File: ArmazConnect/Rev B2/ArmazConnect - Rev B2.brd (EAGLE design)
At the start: 165 x 74 mm, 43 parts, among them X0 NC3FAAV2, X1 NC3FAAV2, X2 NC3FAAV2, X3 NC3FAAV2, X4 NC5FAV-SW, X5 NC5MAV-SW, X6 NC5FAV-SW, X8 87832-26

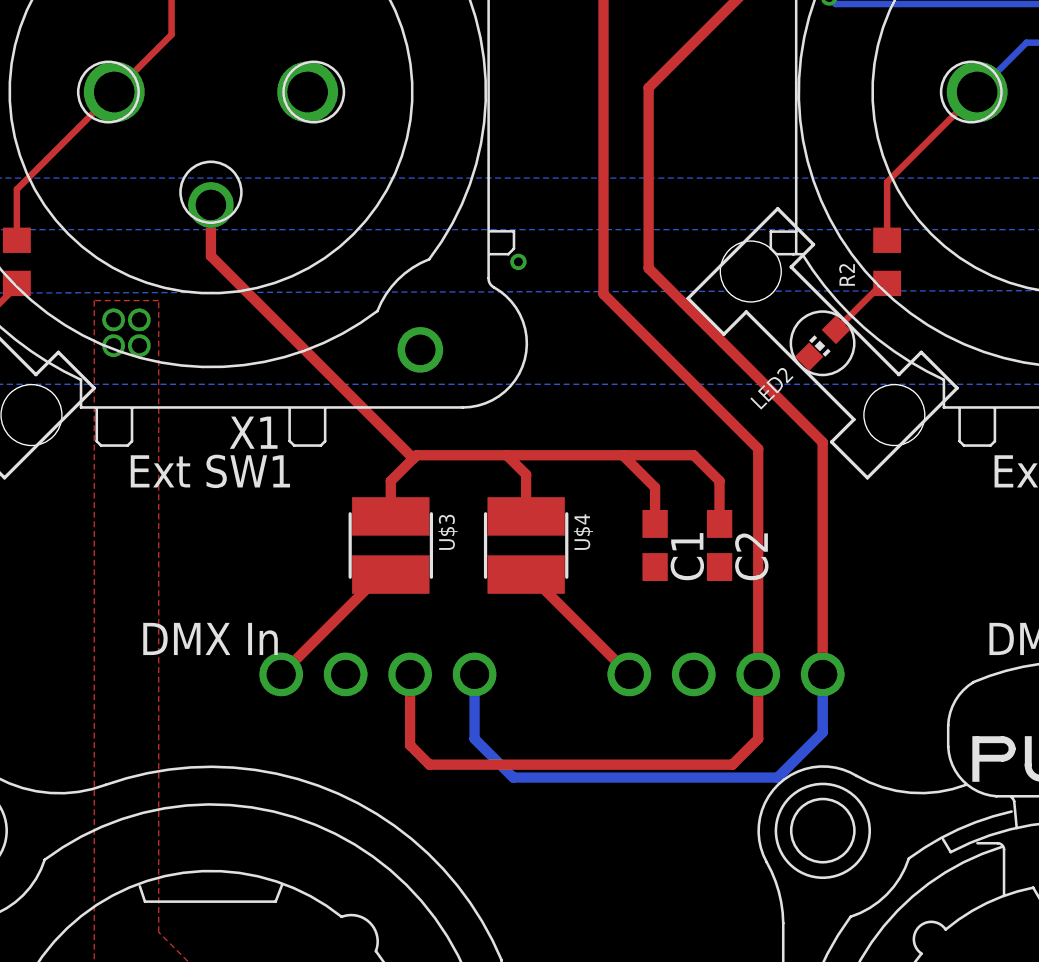
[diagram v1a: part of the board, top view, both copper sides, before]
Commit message: Update routing of ArmazConnect- Rev B2 (creation of polygon for +5V and GND1)
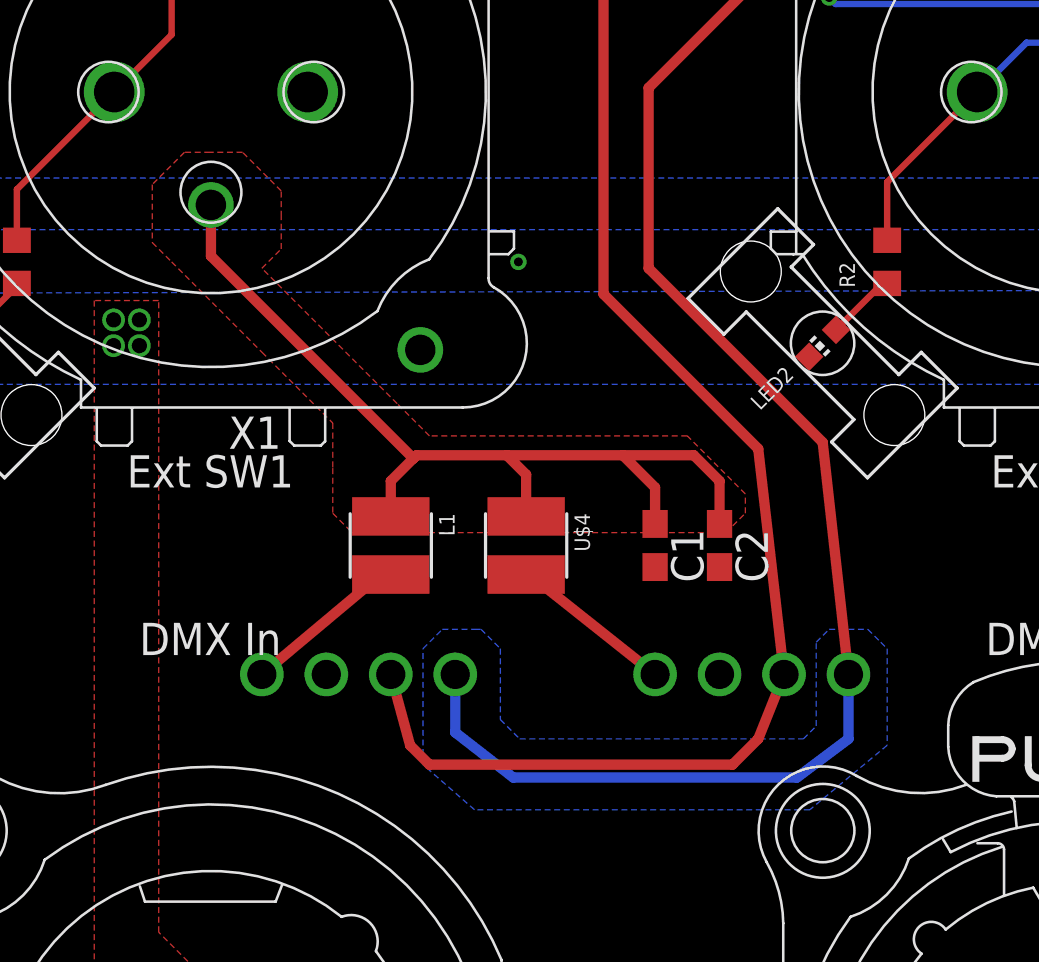
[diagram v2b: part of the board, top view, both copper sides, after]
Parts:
- removed U$1, U$2: MEE3S1205SC, dc-dc-converter:MEE3
- added DC1, DC2: MEE3S1205SC, dc-dc-converter:MEE3
- renumbered U$3 to L1
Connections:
- net +12V: now also DC1.2, DC2.2; no longer U$1.2, U$2.2
- net GND: now also DC1.3, DC2.3; no longer U$1.3, U$2.3
- net GND1: now also DC1.1, DC2.1; no longer U$1.1, U$2.1
- net N$5: now also DC1.4; no longer U$1.4
- net N$7: now also DC2.4; no longer U$2.4
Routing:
- net GND1: track 132.7 -> 134.3 mm
- net N$7: track 5.69 -> 6.45 mm
- net N$5: track 5.95 -> 6.51 mm
- added copper zone on layer 16, net GND1
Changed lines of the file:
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@@
 <grid distance="10" unitdist="mil" unit="mil" style="lines" multiple="1" display="no" altdistance="0.5" altunitdist="mm" altunit="mm"/>
 <layers>
-<layer number="1" name="Top" color="4" fill="1" visible="yes" active="yes"/>
+<layer number="1" name="Top" color="4" fill="1" visible="no" active="yes"/>
 <layer number="2" name="Route2" color="1" fill="3" visible="no" active="no"/>
 <layer number="3" name="Route3" color="4" fill="3" visible="no" active="no"/>
@@
 <layer number="19" name="Unrouted" color="6" fill="1" visible="yes" active="yes"/>
 <layer number="20" name="Dimension" color="15" fill="1" visible="yes" active="yes"/>
-<layer number="21" name="tPlace" color="7" fill="1" visible="yes" active="yes"/>
+<layer number="21" name="tPlace" color="7" fill="1" visible="no" active="yes"/>
 <layer number="22" name="bPlace" color="7" fill="1" visible="yes" active="yes"/>
-<layer number="23" name="tOrigins" color="15" fill="1" visible="yes" active="yes"/>
+<layer number="23" name="tOrigins" color="15" fill="1" visible="no" active="yes"/>
 <layer number="24" name="bOrigins" color="15" fill="1" visible="yes" active="yes"/>
-<layer number="25" name="tNames" color="7" fill="1" visible="yes" active="yes"/>
+<layer number="25" name="tNames" color="7" fill="1" visible="no" active="yes"/>
 <layer number="26" name="bNames" color="7" fill="1" visible="yes" active="yes"/>
-<layer number="27" name="tValues" color="7" fill="1" visible="yes" active="yes"/>
+<layer number="27" name="tValues" color="7" fill="1" visible="no" active="yes"/>
 <layer number="28" name="bValues" color="7" fill="1" visible="yes" active="yes"/>
 <layer number="29" name="tStop" color="7" fill="3" visible="no" active="yes"/>
@@
 <layer number="49" name="Reference" color="7" fill="1" visible="yes" active="yes"/>
 <layer number="50" name="dxf" color="7" fill="1" visible="no" active="no"/>
-<layer number="51" name="tDocu" color="7" fill="1" visible="yes" active="yes"/>
+<layer number="51" name="tDocu" color="7" fill="1" visible="no" active="yes"/>
 <layer number="52" name="bDocu" color="7" fill="1" visible="yes" active="yes"/>
 <layer number="53" name="tGND_GNDA" color="7" fill="1" visible="no" active="no"/>
@@
 <attribute name="VALUE" x="136.906" y="57.912" size="0.4064" layer="27" ratio="10"/>
 </element>
-<element name="U$1" library="dc-dc-converter" package="MEE3" value="MEE3S1205SC" x="48.768" y="35.052" rot="MR0"/>
-<element name="U$2" library="dc-dc-converter" package="MEE3" value="MEE3S1205SC" x="62.484" y="35.052" rot="MR0"/>
-<element name="U$3" library="murata-inductance" package="8200" value="10uH" x="53.086" y="40.132" rot="R180"/>
+<element name="DC1" library="dc-dc-converter" package="MEE3" value="MEE3S1205SC" x="48.006" y="35.052" rot="MR0"/>
+<element name="DC2" library="dc-dc-converter" package="MEE3" value="MEE3S1205SC" x="63.5" y="35.052" rot="MR0"/>
+<element name="L1" library="murata-inductance" package="8200" value="10uH" x="53.086" y="40.132" rot="R180"/>
 <element name="U$4" library="murata-inductance" package="8200" value="10uH" x="58.42" y="40.132" rot="R180"/>
 <element name="C1" library="rcl" package="C0603" value="4.7uF" x="63.5" y="40.132" rot="R270"/>
@@
 <contactref element="C1" pad="2"/>
 <contactref element="C2" pad="2"/>
-<contactref element="U$2" pad="3"/>
-<contactref element="U$1" pad="3"/>
+<contactref element="DC2" pad="3"/>
+<contactref element="DC1" pad="3"/>
 </signal>
 <signal name="N$27">
@@
 <wire x1="137.414" y1="59.248" x2="137.8" y2="59.248" width="0.4064" layer="1"/>
 <wire x1="137.8" y1="59.248" x2="137.822" y2="59.27" width="0.4064" layer="1"/>
-<contactref element="U$3" pad="2"/>
+<contactref element="L1" pad="2"/>
 <contactref element="U$4" pad="2"/>
 <contactref element="C2" pad="1"/>
@@
 <wire x1="46" y1="53.55" x2="46" y2="51.536" width="0.4064" layer="1"/>
 <wire x1="46" y1="51.536" x2="53.975" y2="43.561" width="0.4064" layer="1"/>
+<polygon width="0.4064" layer="1">
+<vertex x="45.974" y="55.626"/>
+<vertex x="44.958" y="55.626"/>
+<vertex x="43.688" y="54.356"/>
+<vertex x="43.688" y="52.07"/>
+<vertex x="44.45" y="51.308"/>
+<vertex x="48.006" y="47.752"/>
+<vertex x="50.8" y="44.958"/>
+<vertex x="50.8" y="43.18"/>
+<vertex x="50.8" y="41.402"/>
+<vertex x="51.562" y="40.64"/>
+<vertex x="65.786" y="40.64"/>
+<vertex x="66.294" y="40.64"/>
+<vertex x="67.056" y="41.402"/>
+<vertex x="67.056" y="42.164"/>
+<vertex x="64.77" y="44.45"/>
+<vertex x="54.61" y="44.45"/>
+<vertex x="53.34" y="45.72"/>
+<vertex x="48.006" y="51.054"/>
+<vertex x="48.768" y="51.816"/>
+<vertex x="48.768" y="53.086"/>
+<vertex x="48.768" y="54.102"/>
+<vertex x="47.244" y="55.626"/>
+</polygon>
 </signal>
 <signal name="ESW0">
@@
 <via x="72.39" y="70.104" extent="1-16" drill="0.35" shape="square"/>
 <via x="71.628" y="70.104" extent="1-16" drill="0.35" shape="square"/>
-<contactref element="U$1" pad="2"/>
-<contactref element="U$2" pad="2"/>
-<wire x1="53.848" y1="35.052" x2="53.848" y2="32.258" width="0.4064" layer="1"/>
+<contactref element="DC1" pad="2"/>
+<contactref element="DC2" pad="2"/>
+<wire x1="53.086" y1="35.052" x2="53.848" y2="32.258" width="0.4064" layer="1"/>
 <wire x1="53.848" y1="32.258" x2="54.61" y2="31.496" width="0.4064" layer="1"/>
 <wire x1="54.61" y1="31.496" x2="66.548" y2="31.496" width="0.4064" layer="1"/>
 <wire x1="66.548" y1="31.496" x2="67.564" y2="32.512" width="0.4064" layer="1"/>
-<wire x1="67.564" y1="32.512" x2="67.564" y2="35.052" width="0.4064" layer="1"/>
-<wire x1="67.564" y1="35.052" x2="67.564" y2="43.942" width="0.4064" layer="1"/>
+<wire x1="67.564" y1="32.512" x2="68.58" y2="35.052" width="0.4064" layer="1"/>
+<wire x1="68.58" y1="35.052" x2="67.564" y2="43.942" width="0.4064" layer="1"/>
 <wire x1="67.564" y1="43.942" x2="61.468" y2="50.038" width="0.4064" layer="1"/>
 <wire x1="61.468" y1="50.038" x2="61.468" y2="69.85" width="0.4064" layer="1"/>
@@
 <wire x1="68.508" y1="63.246" x2="68" y2="63.754" width="0.4064" layer="16"/>
 <via x="68" y="63.754" extent="1-16" drill="0.35"/>
-<contactref element="U$1" pad="1"/>
-<contactref element="U$2" pad="1"/>
-<wire x1="56.388" y1="35.052" x2="56.388" y2="32.512" width="0.4064" layer="16"/>
-<wire x1="56.388" y1="32.512" x2="57.912" y2="30.988" width="0.4064" layer="16"/>
-<wire x1="57.912" y1="30.988" x2="68.326" y2="30.988" width="0.4064" layer="16"/>
-<wire x1="68.326" y1="30.988" x2="70.104" y2="32.766" width="0.4064" layer="16"/>
-<wire x1="70.104" y1="32.766" x2="70.104" y2="35.052" width="0.4064" layer="16"/>
-<wire x1="70.104" y1="35.052" x2="70.104" y2="44.196" width="0.4064" layer="1"/>
+<contactref element="DC1" pad="1"/>
+<contactref element="DC2" pad="1"/>
+<wire x1="55.626" y1="35.052" x2="55.626" y2="32.766" width="0.4064" layer="16"/>
+<wire x1="55.626" y1="32.766" x2="57.912" y2="30.988" width="0.4064" layer="16"/>
+<wire x1="57.912" y1="30.988" x2="69.088" y2="30.988" width="0.4064" layer="16"/>
+<wire x1="69.088" y1="30.988" x2="71.12" y2="32.512" width="0.4064" layer="16"/>
+<wire x1="71.12" y1="32.512" x2="71.12" y2="35.052" width="0.4064" layer="16"/>
+<wire x1="71.12" y1="35.052" x2="70.104" y2="44.196" width="0.4064" layer="1"/>
 <wire x1="70.104" y1="44.196" x2="63.246" y2="51.054" width="0.4064" layer="1"/>
 <wire x1="63.246" y1="51.054" x2="63.246" y2="58.166" width="0.4064" layer="1"/>
 <wire x1="68" y1="63.754" x2="68" y2="62.92" width="0.4064" layer="1"/>
 <wire x1="68" y1="62.92" x2="63.246" y2="58.166" width="0.4064" layer="1"/>
+<polygon width="0.4064" layer="16">
+<vertex x="55.118" y="36.83"/>
+<vertex x="56.388" y="36.83"/>
+<vertex x="56.642" y="36.83"/>
+<vertex x="57.404" y="36.068"/>
+<vertex x="57.404" y="33.274"/>
+<vertex x="58.166" y="32.512"/>
+<vertex x="69.342" y="32.512"/>
+<vertex x="69.85" y="33.02"/>
+<vertex x="69.85" y="36.322"/>
+<vertex x="70.358" y="36.83"/>
+<vertex x="71.882" y="36.83"/>
+<vertex x="72.39" y="36.322"/>
+<vertex x="72.644" y="36.068"/>
+<vertex x="72.644" y="32.258"/>
+<vertex x="69.596" y="29.718"/>
+<vertex x="56.388" y="29.718"/>
+<vertex x="54.356" y="31.496"/>
+<vertex x="54.356" y="36.068"/>
+</polygon>
 </signal>
 <signal name="FAN0_GND" class="1">
@@
 </signal>
 <signal name="N$5">
-<contactref element="U$1" pad="4"/>
-<contactref element="U$3" pad="1"/>
+<contactref element="DC1" pad="4"/>
+<contactref element="L1" pad="1"/>
 <wire x1="53.086" y1="38.987" x2="52.703" y2="38.987" width="0.4064" layer="1"/>
-<wire x1="52.703" y1="38.987" x2="48.768" y2="35.052" width="0.4064" layer="1"/>
+<wire x1="52.703" y1="38.987" x2="48.006" y2="35.052" width="0.4064" layer="1"/>
 </signal>
 <signal name="N$7">
 <contactref element="U$4" pad="1"/>
-<contactref element="U$2" pad="4"/>
+<contactref element="DC2" pad="4"/>
 <wire x1="58.42" y1="38.987" x2="58.549" y2="38.987" width="0.4064" layer="1"/>
-<wire x1="58.549" y1="38.987" x2="62.484" y2="35.052" width="0.4064" layer="1"/>
+<wire x1="58.549" y1="38.987" x2="63.5" y2="35.052" width="0.4064" layer="1"/>
 </signal>
 </signals>

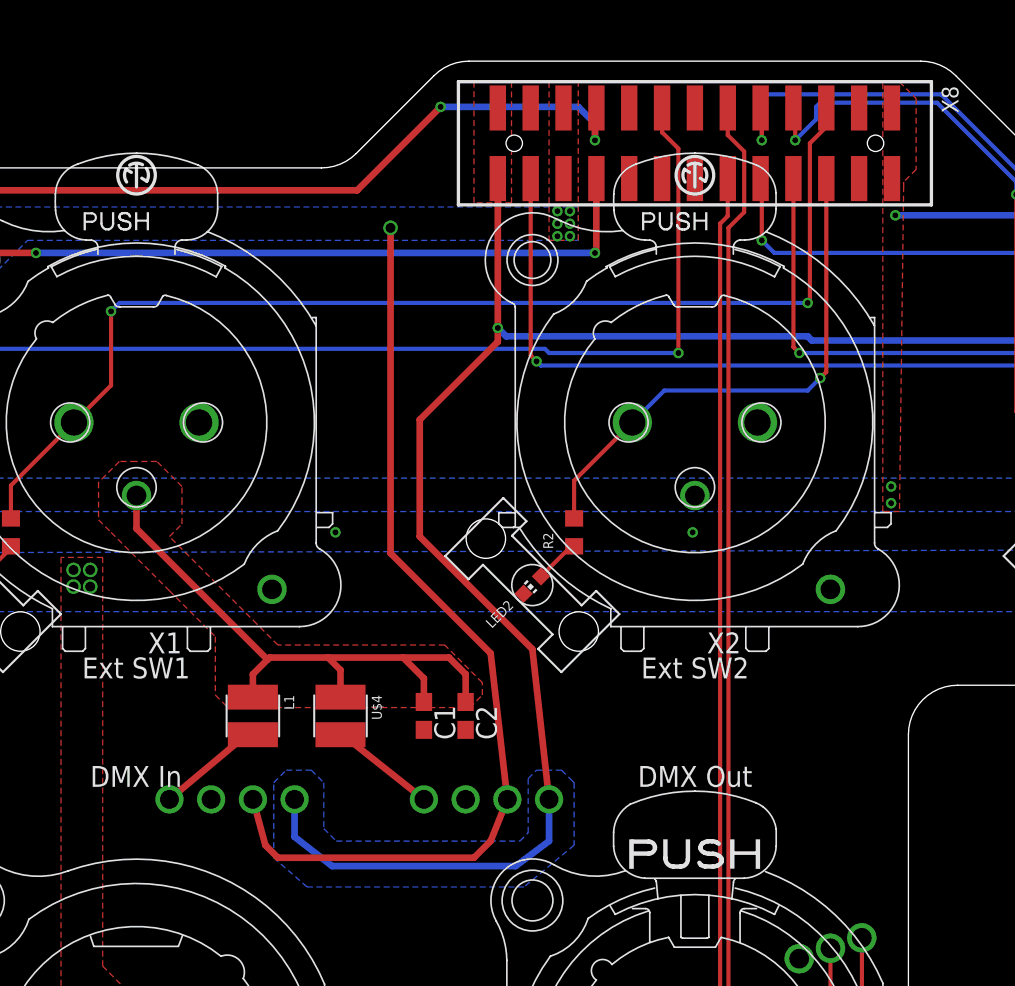
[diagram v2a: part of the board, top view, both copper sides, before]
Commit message: Routing proposal for DC/DC converters on ArmazConnect - Rev B2
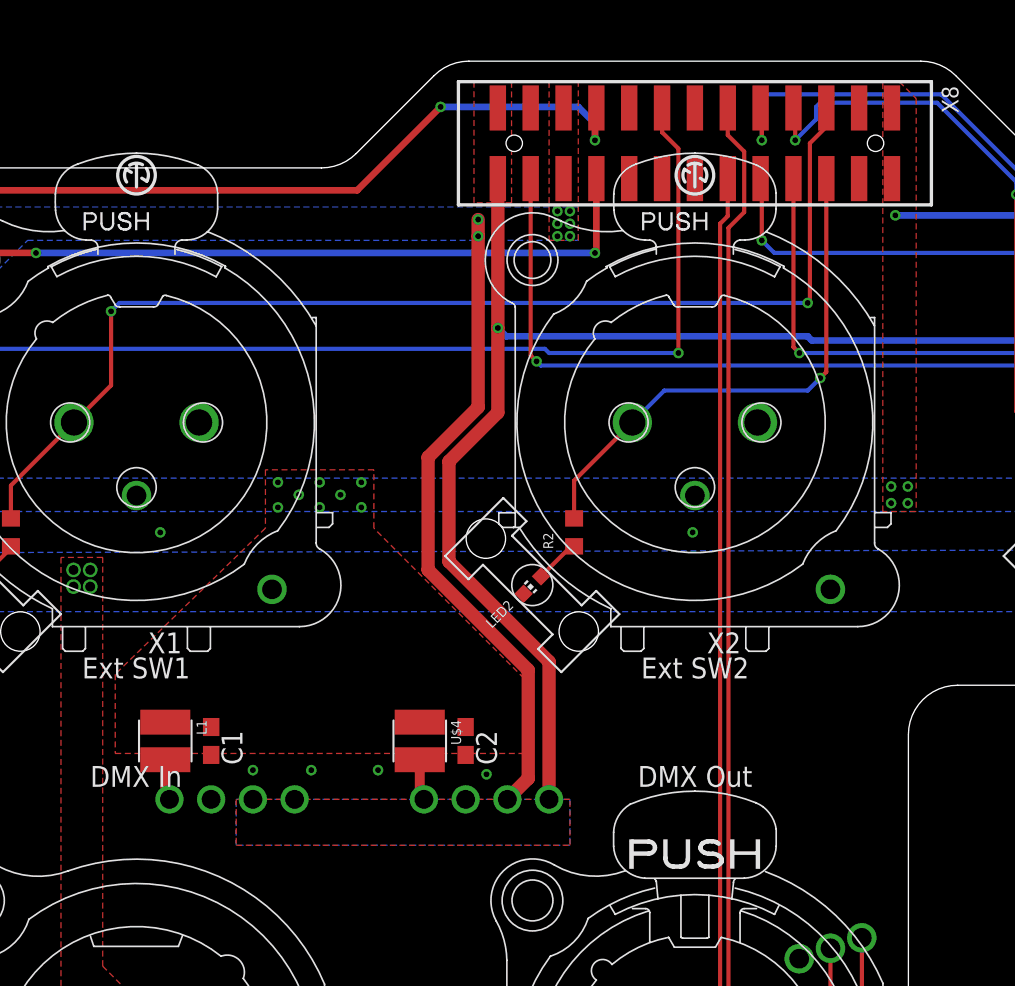
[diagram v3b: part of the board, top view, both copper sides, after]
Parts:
- moved C1 13.0 mm to (50.5, 38.6)
- moved L1 5.55 mm to (47.8, 38.6)
- moved U$4 5.06 mm to (63.2, 38.6)
- moved C2 1.52 mm to (66.0, 38.6)
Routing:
- net +5V: track 69.6 -> 33.5 mm, vias 3 -> 13
- net GND1: track 134.3 -> 111.7 mm
- net +12V: track 57.5 -> 39.6 mm, vias 7 -> 8
- net N$5: track 6.51 -> 2.52 mm
- net N$7: track 6.45 -> 2.52 mm

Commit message: dc-dc-converter.lbr updated. Fiducials added. Silkscreen improved.
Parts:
- added FI1, FI2, FI3, FI4, FI5, FI6, FI7, FI8: FIDUCIAL1X2, SparkFun:FIDUCIAL-1X2
- added U$1: EXMACHINA-LOGO-NAME, exmachina:EXM-LOGO-BASELINE
- added U$2: CC-BY-SA, cc-by-sa:CC-BY-SA
- X0, X1, X2, X3: value NC3FAAV2 -> NC3FAV2
- moved DC1 3.81 mm to (51.8, 35.1)
- moved DC2 3.81 mm to (67.3, 35.1)
- renumbered U$4 to L2
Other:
- board text added: "ArmazConnect Rev B2"
